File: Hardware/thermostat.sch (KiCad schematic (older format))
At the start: 5 parts

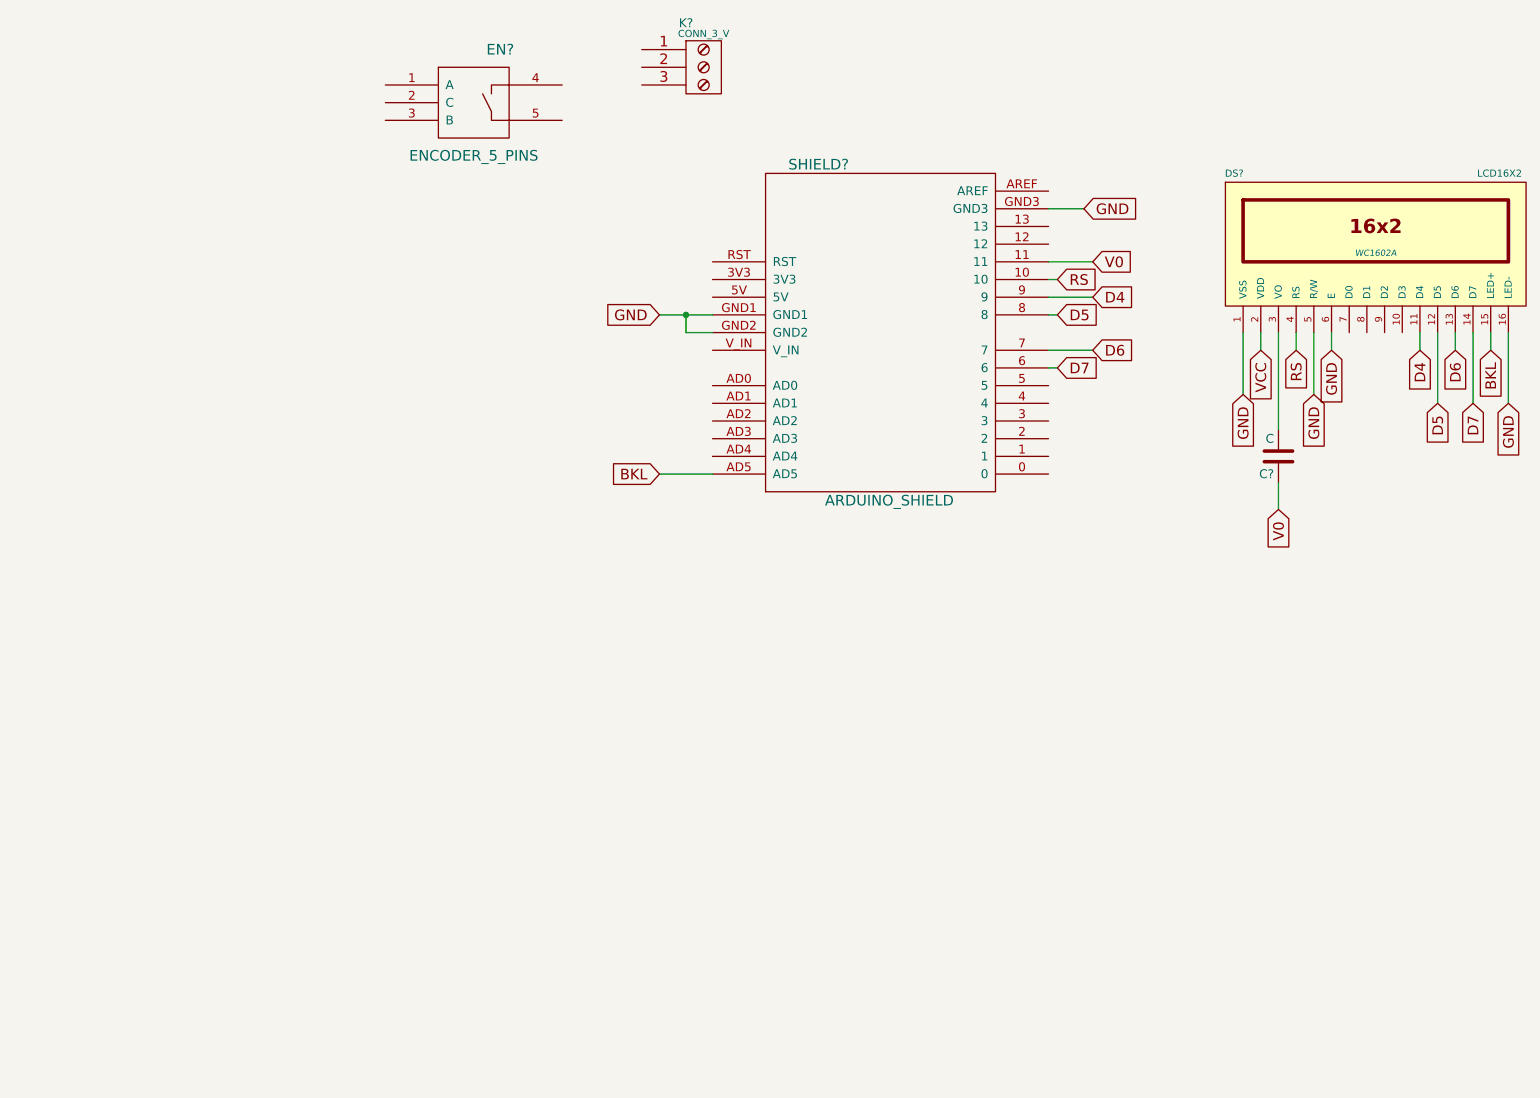
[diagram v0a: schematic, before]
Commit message: Added encoder
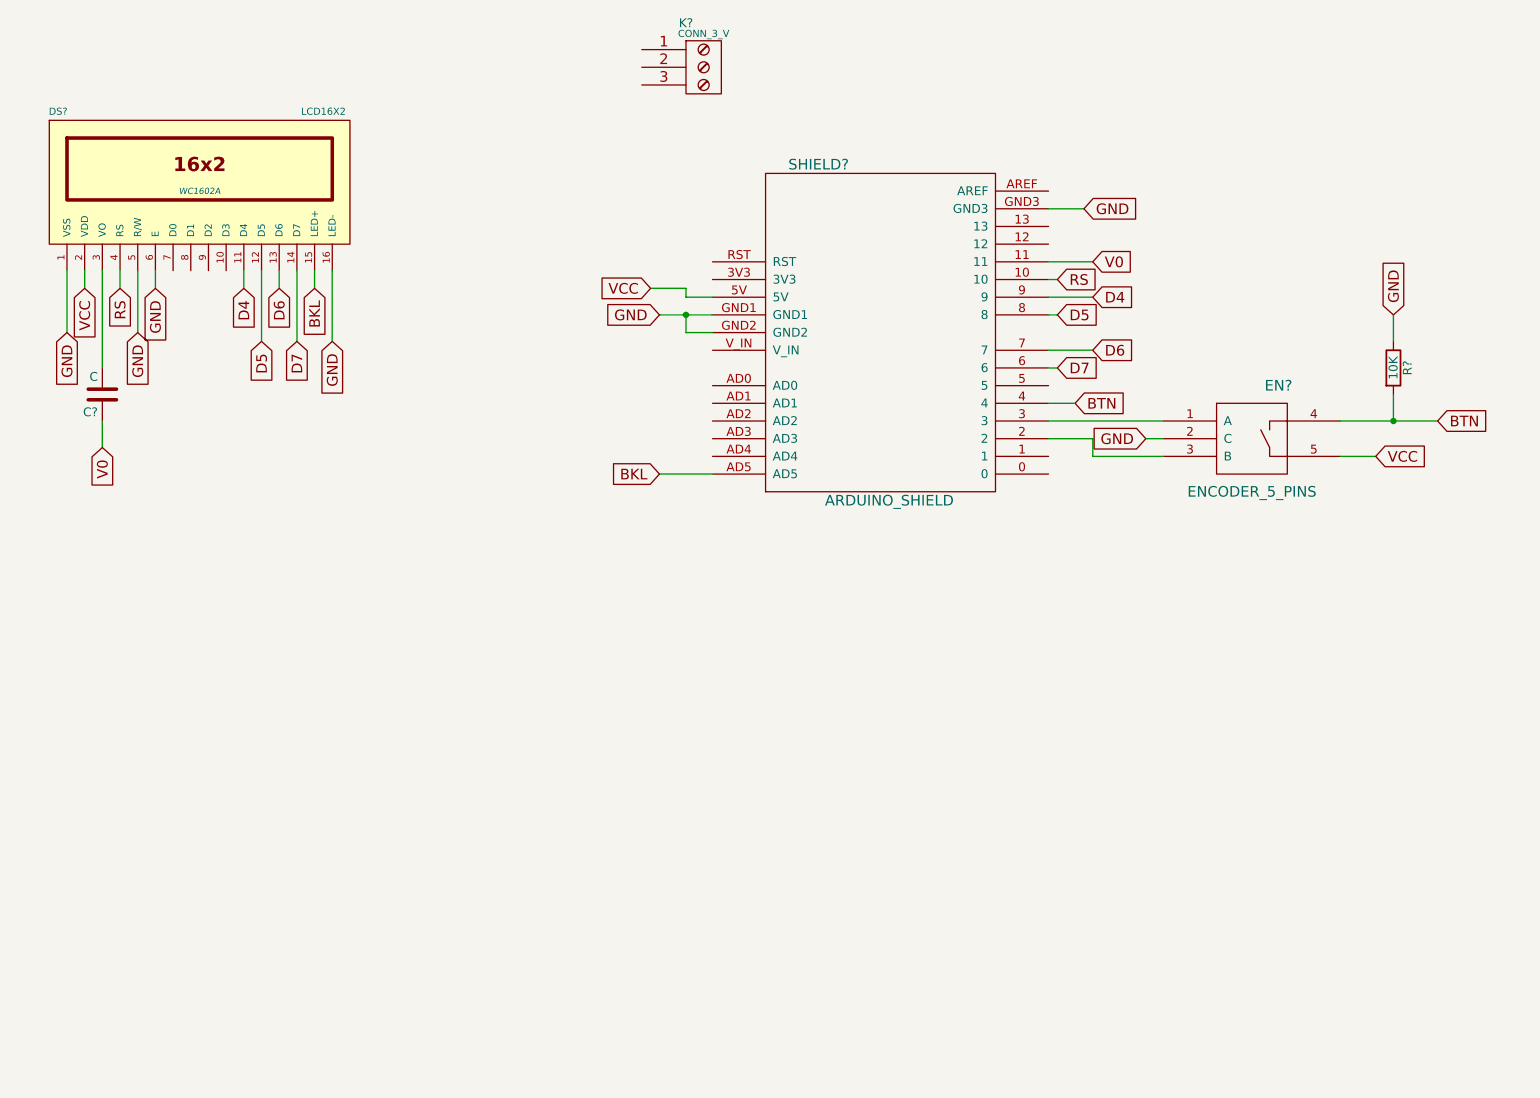
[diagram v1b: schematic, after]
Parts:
- added R?: 10K, symbol R
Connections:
- net GND: now also EN?.2 (C), R?.1
- net VCC: now also EN?.5, SHIELD?.5V
- net at SHIELD?.2: now also EN?.3 (B)
- net at SHIELD?.3: now also EN?.1 (A)
- net BTN: now reaches SHIELD?.4
- net BTN: now also EN?.4, R?.2
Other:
- moved on the sheet: C?, DS?, EN?
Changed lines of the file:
@@
 L LCD16X2 DS?
 U 1 1 55D36442
-P 8850 2150
-F 0 "DS?" H 8050 2550 40  0000 C CNN
-F 1 "LCD16X2" H 9550 2550 40  0000 C CNN
-F 2 "WC1602A" H 8850 2100 35  0000 C CIN
-F 3 "" H 8850 2150 60  0000 C CNN
-	1    8850 2150
+P 2200 1800
+F 0 "DS?" H 1400 2200 40  0000 C CNN
+F 1 "LCD16X2" H 2900 2200 40  0000 C CNN
+F 2 "WC1602A" H 2200 1750 35  0000 C CIN
+F 3 "" H 2200 1800 60  0000 C CNN
+	1    2200 1800
 	1    0    0    -1
 $EndComp
@@
 L ENCODER_5_PINS EN?
 U 1 1 55D365E3
-P 3750 1350
-F 0 "EN?" H 3900 1650 60  0000 C CNN
-F 1 "ENCODER_5_PINS" H 3750 1050 60  0000 C CNN
-F 2 "" H 3750 1350 60  0000 C CNN
-F 3 "" H 3750 1350 60  0000 C CNN
-	1    3750 1350
+P 8150 3250
+F 0 "EN?" H 8300 3550 60  0000 C CNN
+F 1 "ENCODER_5_PINS" H 8150 2950 60  0000 C CNN
+F 2 "" H 8150 3250 60  0000 C CNN
+F 3 "" H 8150 3250 60  0000 C CNN
+	1    8150 3250
 	1    0    0    -1
 $EndComp
@@
 L C C?
 U 1 1 55D43036
-P 8300 3350
-F 0 "C?" H 8325 3450 50  0000 L CNN
-F 1 "C" H 8325 3250 50  0000 L CNN
-F 2 "" H 8338 3200 30  0000 C CNN
-F 3 "" H 8300 3350 60  0000 C CNN
-	1    8300 3350
+P 1650 3000
+F 0 "C?" H 1675 3100 50  0000 L CNN
+F 1 "C" H 1675 2900 50  0000 L CNN
+F 2 "" H 1688 2850 30  0000 C CNN
+F 3 "" H 1650 3000 60  0000 C CNN
+	1    1650 3000
 	-1   0    0    1
 $EndComp
-Text GLabel 8300 3650 3    60   Input ~ 0
+Text GLabel 1650 3300 3    60   Input ~ 0
 V0
 Text GLabel 7250 2250 2    60   Input ~ 0
 V0
-Text GLabel 8100 3000 3    60   Input ~ 0
+Text GLabel 1450 2650 3    60   Input ~ 0
 GND
-Text GLabel 8200 2750 3    60   Input ~ 0
+Text GLabel 1550 2400 3    60   Input ~ 0
 VCC
-Text GLabel 8400 2750 3    60   Input ~ 0
+Text GLabel 1750 2400 3    60   Input ~ 0
 RS
 Text GLabel 7050 2350 2    60   Input ~ 0
 RS
-Text GLabel 8500 3000 3    60   Input ~ 0
+Text GLabel 1850 2650 3    60   Input ~ 0
 GND
-Text GLabel 8600 2750 3    60   Input ~ 0
+Text GLabel 1950 2400 3    60   Input ~ 0
 GND
-Text GLabel 9100 2750 3    60   Input ~ 0
+Text GLabel 2450 2400 3    60   Input ~ 0
 D4
 Text GLabel 7250 2450 2    60   Input ~ 0
 D4
-Text GLabel 9200 3050 3    60   Input ~ 0
+Text GLabel 2550 2700 3    60   Input ~ 0
 D5
-Text GLabel 9300 2750 3    60   Input ~ 0
+Text GLabel 2650 2400 3    60   Input ~ 0
 D6
-Text GLabel 9400 3050 3    60   Input ~ 0
+Text GLabel 2750 2700 3    60   Input ~ 0
 D7
 Text GLabel 7050 2550 2    60   Input ~ 0
@@
 Text GLabel 7050 2850 2    60   Input ~ 0
 D7
-Text GLabel 9600 3050 3    60   Input ~ 0
+Text GLabel 2950 2700 3    60   Input ~ 0
 GND
-Text GLabel 9500 2750 3    60   Input ~ 0
+Text GLabel 2850 2400 3    60   Input ~ 0
 BKL
 Wire Wire Line
-	8300 2650 8300 3200
+	1650 2300 1650 2850
 Wire Wire Line
-	8300 3650 8300 3500
+	1650 3300 1650 3150
 Wire Wire Line
 	7250 2250 7000 2250
 Wire Wire Line
-	8100 2650 8100 3000
+	1450 2300 1450 2650
 Wire Wire Line
-	8200 2750 8200 2650
+	1550 2400 1550 2300
 Wire Wire Line
-	8400 2750 8400 2650
+	1750 2400 1750 2300
 Wire Wire Line
 	7050 2350 7000 2350
 Wire Wire Line
-	8500 3000 8500 2650
+	1850 2650 1850 2300
 Wire Wire Line
-	8600 2750 8600 2650
+	1950 2400 1950 2300
 Wire Wire Line
-	9100 2750 9100 2650
+	2450 2400 2450 2300
 Wire Wire Line
 	7250 2450 7000 2450
 Wire Wire Line
-	9200 2650 9200 3050
+	2550 2300 2550 2700
 Wire Wire Line
-	9300 2750 9300 2650
+	2650 2400 2650 2300
 Wire Wire Line
-	9400 2650 9400 3050
+	2750 2300 2750 2700
 Wire Wire Line
 	7050 2550 7000 2550
@@
 	7050 2850 7000 2850
 Wire Wire Line
-	9600 2650 9600 3050
+	2950 2300 2950 2700
 Wire Wire Line
-	9500 2750 9500 2650
+	2850 2400 2850 2300
 Text GLabel 4800 3450 0    60   Input ~ 0
 BKL
@@
 Wire Wire Line
 	7200 1950 7000 1950
+Wire Wire Line
+	7650 3150 7000 3150
+Wire Wire Line
+	7650 3350 7250 3350
+Wire Wire Line
+	7250 3350 7250 3250
+Wire Wire Line
+	7250 3250 7000 3250
+Text GLabel 7550 3250 0    60   Input ~ 0
+GND
+Wire Wire Line
+	7550 3250 7650 3250
+$Comp
+L R R?
+U 1 1 55D49535
+P 8950 2850
+F 0 "R?" V 9030 2850 50  0000 C CNN
+F 1 "10K" V 8950 2850 50  0000 C CNN
+F 2 "" V 8880 2850 30  0000 C CNN
+F 3 "" H 8950 2850 30  0000 C CNN
+	1    8950 2850
+	1    0    0    -1
+$EndComp
+Text GLabel 8950 2550 1    60   Input ~ 0
+GND
+Text GLabel 7150 3050 2    60   Input ~ 0
+BTN
+Wire Wire Line
+	7150 3050 7000 3050
+Text GLabel 9200 3150 2    60   Input ~ 0
+BTN
+Wire Wire Line
+	9200 3150 8650 3150
+Wire Wire Line
+	8950 3150 8950 3000
+Connection ~ 8950 3150
+Wire Wire Line
+	8950 2700 8950 2550
+Text GLabel 4750 2400 0    60   Input ~ 0
+VCC
+Wire Wire Line
+	4750 2400 4950 2400
+Wire Wire Line
+	4950 2400 4950 2450
+Wire Wire Line
+	4950 2450 5100 2450
+Text GLabel 8850 3350 2    60   Input ~ 0
+VCC
+Wire Wire Line
+	8850 3350 8650 3350
 $EndSCHEMATC

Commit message: Added value to pasive parts
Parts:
- C?: value C -> 100uF
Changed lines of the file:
@@
 P 1650 3000
 F 0 "C?" H 1675 3100 50  0000 L CNN
-F 1 "C" H 1675 2900 50  0000 L CNN
+F 1 "100uF" H 1675 2900 50  0000 L CNN
 F 2 "" H 1688 2850 30  0000 C CNN
 F 3 "" H 1650 3000 60  0000 C CNN

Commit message: Removed wrong libraries
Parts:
- added D1: LED, LEDs:LED-3MM, symbol LED
- added P1, P2: CONN_01X01, library:header1x01, symbol CONN_01X01
- added R1: 10K, Resistors_ThroughHole:Resistor_Horizontal_RM10mm, symbol R
- C1: renamed from C?; footprint (none) -> Capacitors_ThroughHole:C_Radial_D10_L13_P5
- DS1: renamed from DS?; footprint WC1602A -> Display:WC1602A
- EN1: renamed from EN?; footprint (none) -> library:ENCODER_5_PINS
- K1: renamed from K?; footprint (none) -> borniers:bornier3_V
- R2: renamed from R?; footprint (none) -> Resistors_ThroughHole:Resistor_Horizontal_RM10mm
- SHIELD1: renamed from SHIELD?; footprint (none) -> arduino_shields:ARDUINO_SHIELD_2
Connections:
- net D4: now also SHIELD1.8; no longer SHIELD1.9
- net D5: now also SHIELD1.9; no longer SHIELD1.8
- net D6: now also SHIELD1.10; no longer SHIELD1.7
- net D7: now also SHIELD1.12; no longer SHIELD1.6
- net GND: now also P1.1 (P1), P2.1 (P1), R1.1; no longer DS1.6 (E)
- net RS: now also SHIELD1.5; no longer SHIELD1.10
- net at SHIELD1.2: now also EN1.1 (A); no longer EN1.3 (B)
- net at SHIELD1.3: now also EN1.3 (B); no longer EN1.1 (A)
- net RELAY: now reaches SHIELD1.AD2
- net RELAY: now also D1.2 (A)
- new net: D1.1 (K), R1.2
- new net E: DS1.6 (E), SHIELD1.6
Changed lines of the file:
@@
 $EndDescr
 $Comp
-L ARDUINO_SHIELD SHIELD?
+L ARDUINO_SHIELD SHIELD1
 U 1 1 55D363D2
 P 6050 2650
-F 0 "SHIELD?" H 5700 3600 60  0000 C CNN
+F 0 "SHIELD1" H 5700 3600 60  0000 C CNN
 F 1 "ARDUINO_SHIELD" H 6100 1700 60  0000 C CNN
-F 2 "" H 6050 2650 60  0000 C CNN
+F 2 "arduino_shields:ARDUINO_SHIELD_2" H 6050 2650 60  0001 C CNN
 F 3 "" H 6050 2650 60  0000 C CNN
 	1    6050 2650
@@
 $EndComp
 $Comp
-L LCD16X2 DS?
+L LCD16X2 DS1
 U 1 1 55D36442
 P 2200 1800
-F 0 "DS?" H 1400 2200 40  0000 C CNN
+F 0 "DS1" H 1400 2200 40  0000 C CNN
 F 1 "LCD16X2" H 2900 2200 40  0000 C CNN
-F 2 "WC1602A" H 2200 1750 35  0000 C CIN
+F 2 "Display:WC1602A" H 2200 1750 35  0000 C CIN
 F 3 "" H 2200 1800 60  0000 C CNN
 	1    2200 1800
@@
 $EndComp
 $Comp
-L ENCODER_5_PINS EN?
+L ENCODER_5_PINS EN1
 U 1 1 55D365E3
 P 8150 3250
-F 0 "EN?" H 8300 3550 60  0000 C CNN
+F 0 "EN1" H 8300 3550 60  0000 C CNN
 F 1 "ENCODER_5_PINS" H 8150 2950 60  0000 C CNN
-F 2 "" H 8150 3250 60  0000 C CNN
+F 2 "library:ENCODER_5_PINS" H 8150 3250 60  0001 C CNN
 F 3 "" H 8150 3250 60  0000 C CNN
 	1    8150 3250
@@
 $EndComp
 $Comp
-L CONN_3_V K?
+L CONN_3_V K1
 U 1 1 55D36620
 P 5050 1150
-F 0 "K?" H 4950 1400 50  0000 C CNN
+F 0 "K1" H 4950 1400 50  0000 C CNN
 F 1 "CONN_3_V" H 5050 1340 40  0000 C CNN
-F 2 "" H 5050 1150 60  0000 C CNN
+F 2 "borniers:bornier3_V" H 5050 1150 60  0001 C CNN
 F 3 "" H 5050 1150 60  0000 C CNN
 	1    5050 1150
@@
 $EndComp
 $Comp
-L C C?
+L C C1
 U 1 1 55D43036
 P 1650 3000
-F 0 "C?" H 1675 3100 50  0000 L CNN
+F 0 "C1" H 1675 3100 50  0000 L CNN
 F 1 "100uF" H 1675 2900 50  0000 L CNN
-F 2 "" H 1688 2850 30  0000 C CNN
+F 2 "Capacitors_ThroughHole:C_Radial_D10_L13_P5" H 1688 2850 30  0001 C CNN
 F 3 "" H 1650 3000 60  0000 C CNN
 	1    1650 3000
@@
 Text GLabel 1750 2400 3    60   Input ~ 0
 RS
-Text GLabel 7050 2350 2    60   Input ~ 0
+Text GLabel 7300 2950 2    60   Input ~ 0
 RS
 Text GLabel 1850 2650 3    60   Input ~ 0
 GND
 Text GLabel 1950 2400 3    60   Input ~ 0
-GND
+E
 Text GLabel 2450 2400 3    60   Input ~ 0
 D4
-Text GLabel 7250 2450 2    60   Input ~ 0
+Text GLabel 7050 2550 2    60   Input ~ 0
 D4
 Text GLabel 2550 2700 3    60   Input ~ 0
@@
 Text GLabel 2750 2700 3    60   Input ~ 0
 D7
-Text GLabel 7050 2550 2    60   Input ~ 0
+Text GLabel 7250 2450 2    60   Input ~ 0
 D5
-Text GLabel 7250 2750 2    60   Input ~ 0
+Text GLabel 7050 2350 2    60   Input ~ 0
 D6
-Text GLabel 7050 2850 2    60   Input ~ 0
-D7
 Text GLabel 2950 2700 3    60   Input ~ 0
 GND
@@
 	7200 1950 7000 1950
 Wire Wire Line
-	7650 3150 7000 3150
-Wire Wire Line
-	7650 3350 7250 3350
-Wire Wire Line
-	7250 3350 7250 3250
-Wire Wire Line
-	7250 3250 7000 3250
+	7050 3350 7650 3350
 Text GLabel 7550 3250 0    60   Input ~ 0
 GND
@@
 	7550 3250 7650 3250
 $Comp
-L R R?
+L R R2
 U 1 1 55D49535
 P 8950 2850
-F 0 "R?" V 9030 2850 50  0000 C CNN
+F 0 "R2" V 9030 2850 50  0000 C CNN
 F 1 "10K" V 8950 2850 50  0000 C CNN
-F 2 "" V 8880 2850 30  0000 C CNN
+F 2 "Resistors_ThroughHole:Resistor_Horizontal_RM10mm" V 8880 2850 30  0001 C CNN
 F 3 "" H 8950 2850 30  0000 C CNN
 	1    8950 2850
@@
 Wire Wire Line
 	8850 3350 8650 3350
+$Comp
+L R R1
+U 1 1 55D4AA7B
+P 2300 4600
+F 0 "R1" V 2380 4600 50  0000 C CNN
+F 1 "10K" V 2300 4600 50  0000 C CNN
+F 2 "Resistors_ThroughHole:Resistor_Horizontal_RM10mm" V 2230 4600 30  0001 C CNN
+F 3 "" H 2300 4600 30  0000 C CNN
+	1    2300 4600
+	1    0    0    -1
+$EndComp
+Text GLabel 2300 4300 1    60   Input ~ 0
+GND
+Wire Wire Line
+	2300 4450 2300 4300
+$Comp
+L LED D1
+U 1 1 55D4AB4B
+P 2300 5100
+F 0 "D1" H 2300 5200 50  0000 C CNN
+F 1 "LED" H 2300 5000 50  0000 C CNN
+F 2 "LEDs:LED-3MM" H 2300 5100 60  0001 C CNN
+F 3 "" H 2300 5100 60  0000 C CNN
+	1    2300 5100
+	0    1    1    0
+$EndComp
+Wire Wire Line
+	2300 4900 2300 4750
+Text GLabel 4800 3150 0    60   Input ~ 0
+RELAY
+Wire Wire Line
+	4800 3150 5100 3150
+Text GLabel 2300 5450 3    60   Input ~ 0
+RELAY
+Wire Wire Line
+	2300 5450 2300 5300
+Wire Wire Line
+	7000 3250 7150 3250
+Wire Wire Line
+	7150 3250 7150 3150
+Wire Wire Line
+	7150 3150 7650 3150
+Wire Wire Line
+	7050 3350 7050 3150
+Wire Wire Line
+	7050 3150 7000 3150
+Text GLabel 7000 2150 2    60   Input ~ 0
+D7
+Wire Wire Line
+	7300 2950 7000 2950
+Text GLabel 7050 2850 2    60   Input ~ 0
+E
+$Comp
+L CONN_01X01 P2
+U 1 1 55D4C211
+P 9000 1400
+F 0 "P2" H 9000 1500 50  0000 C CNN
+F 1 "CONN_01X01" V 9100 1400 50  0000 C CNN
+F 2 "library:header1x01" H 9000 1400 60  0001 C CNN
+F 3 "" H 9000 1400 60  0000 C CNN
+	1    9000 1400
+	1    0    0    -1
+$EndComp
+$Comp
+L CONN_01X01 P1
+U 1 1 55D4C277
+P 8300 1400
+F 0 "P1" H 8300 1500 50  0000 C CNN
+F 1 "CONN_01X01" V 8400 1400 50  0000 C CNN
+F 2 "library:header1x01" H 8300 1400 60  0001 C CNN
+F 3 "" H 8300 1400 60  0000 C CNN
+	1    8300 1400
+	-1   0    0    1
+$EndComp
+Wire Wire Line
+	8500 1400 8800 1400
+Text GLabel 8650 1350 1    60   Input ~ 0
+GND
+Wire Wire Line
+	8650 1350 8650 1400
+Connection ~ 8650 1400
 $EndSCHEMATC
